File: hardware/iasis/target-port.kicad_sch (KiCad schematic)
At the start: 0 parts

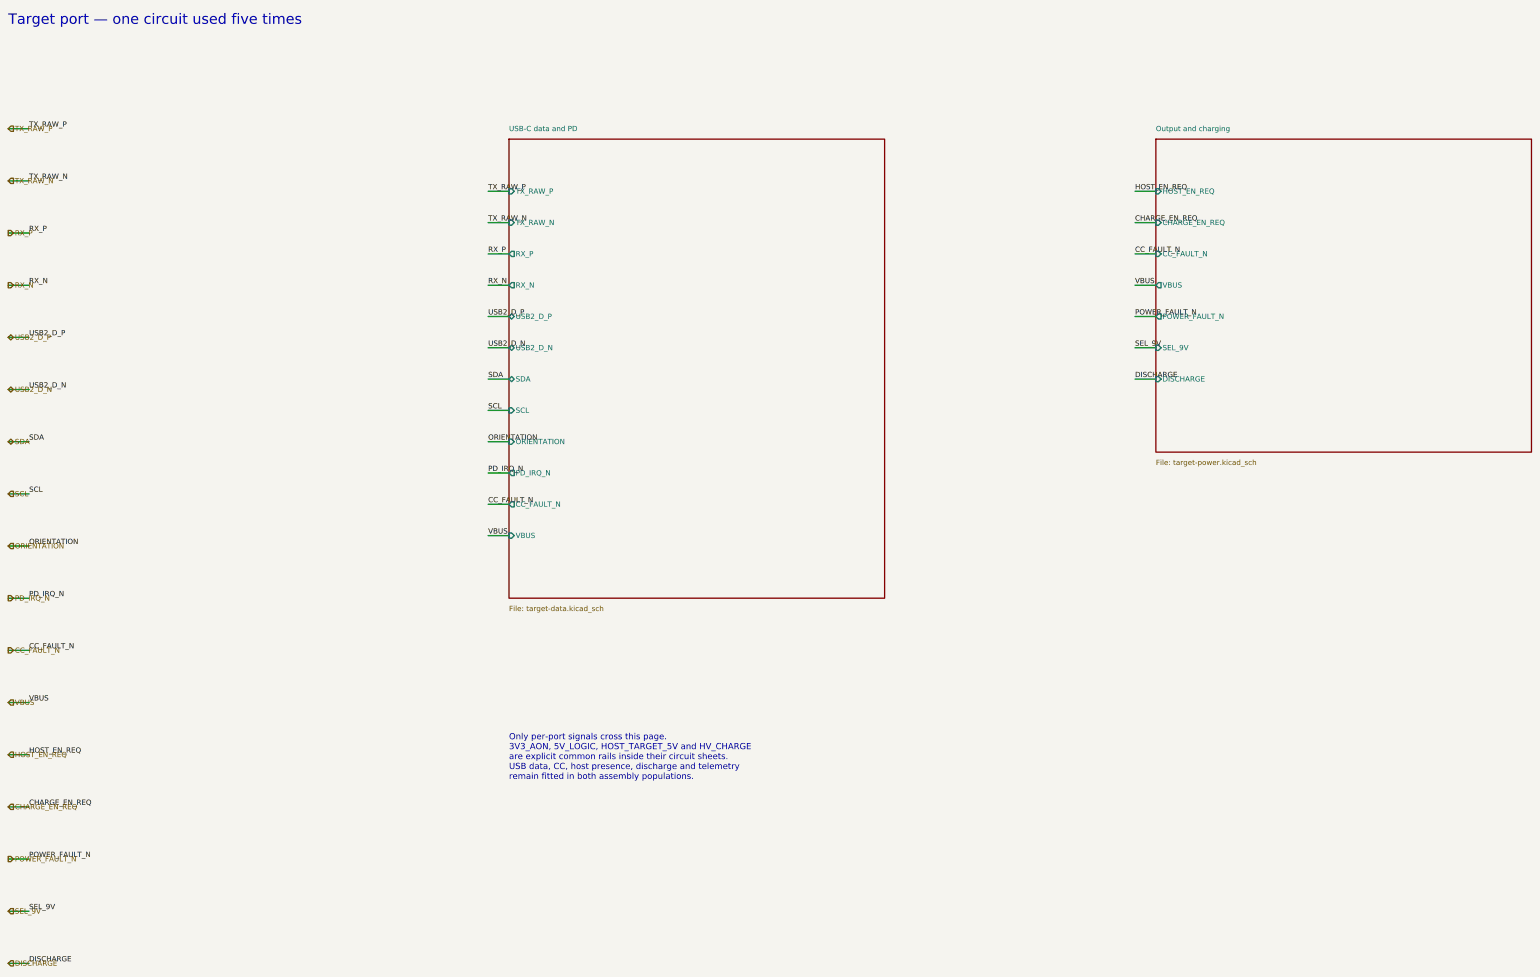
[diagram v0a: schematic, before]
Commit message: Add the CM5 carrier design for reference
The first board revision: a Raspberry Pi CM5 carrier with M.2 NVMe,
Ethernet and five USB 3 and USB-PD ports, as it stood before the compact
hub replaced it, squashed from 45 commits.
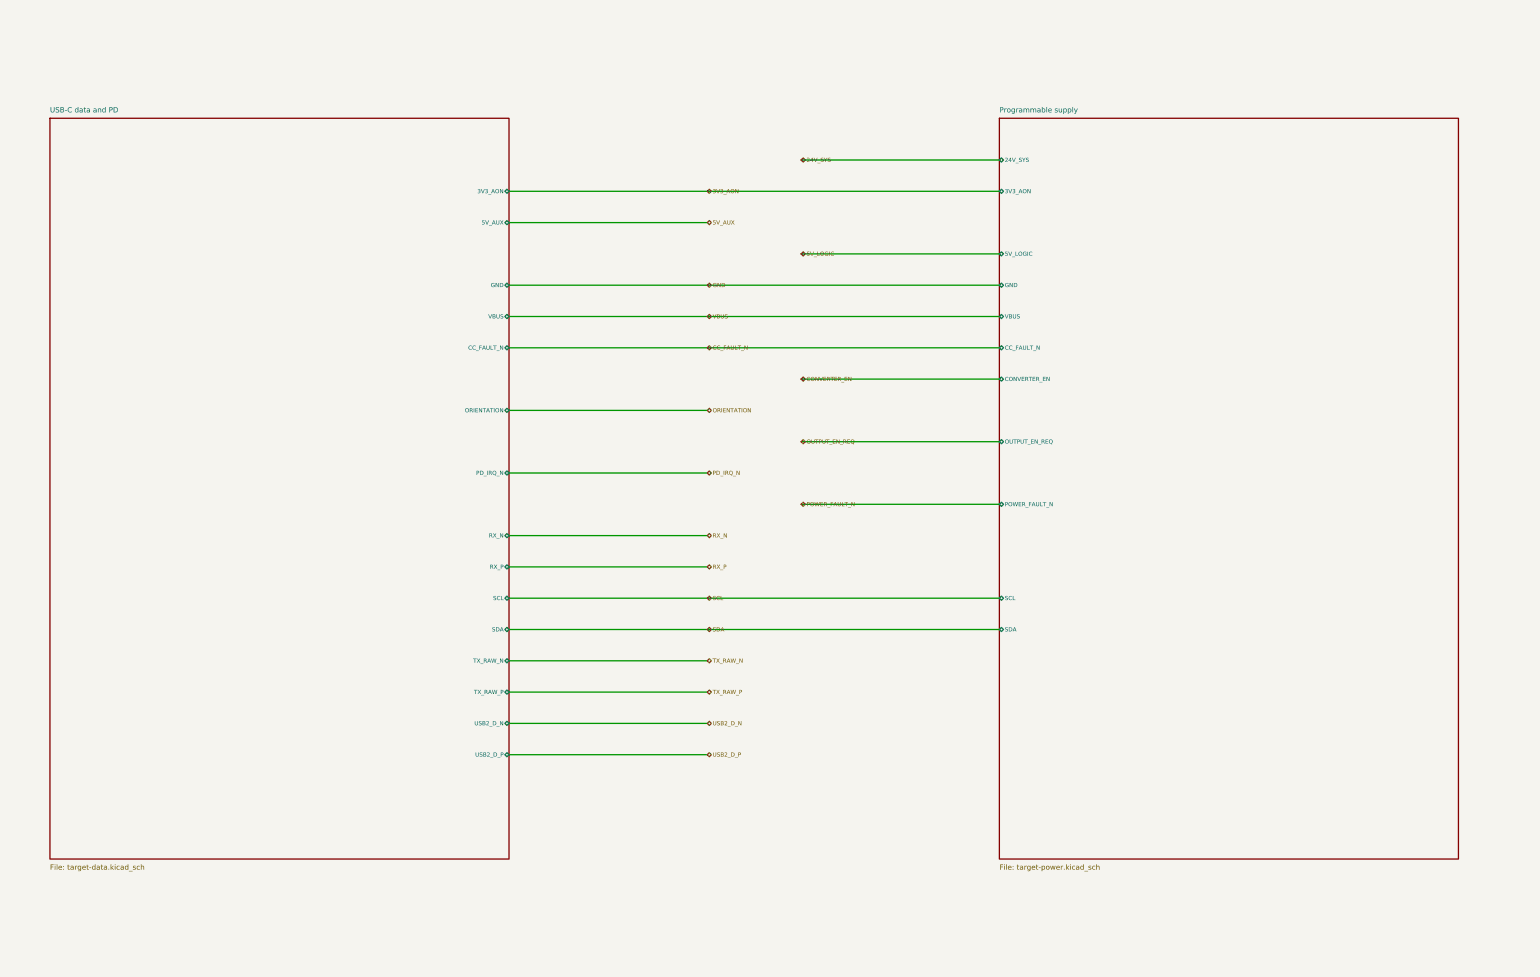
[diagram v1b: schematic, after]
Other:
- sheet Output and charging renamed Programmable supply
- sheet Programmable supply ports: added 24V_SYS, 3V3_AON, 5V_LOGIC, CONVERTER_EN, GND, OUTPUT_EN_REQ, SCL, SDA; removed CHARGE_EN_REQ, DISCHARGE, HOST_EN_REQ, SEL_9V
- sheet USB-C data and PD ports: added 3V3_AON, 5V_AUX, GND; removed none
- note removed: "Only per-port signals cross this page. 3V3_AON, 5V_LOGIC, HOST_TARGET_5V and HV_CHARGE are explicit common rails inside their circuit sheets. USB data, CC, host presence, discharge and telemetry remain fitted in both assembly populations."
- note removed: "Target port — one circuit used five times"
- title: (none) -> Target port
